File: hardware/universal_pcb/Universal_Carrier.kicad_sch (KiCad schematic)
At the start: 20 parts, among them J1 ESP32_T_LANDSCAPE, J11 PWR_ESP_5V, J12 PWR_SERVO_5V, J2 ESP32_B_LANDSCAPE, J3 SX1278_LORA_2x4, J4 BATT_APM, J5 DETECTOR_ANCORA, J6 GPS_LC29H_7PIN, SW1 UP, SW2 MODE, SW3 DOWN, SW4 BOOT

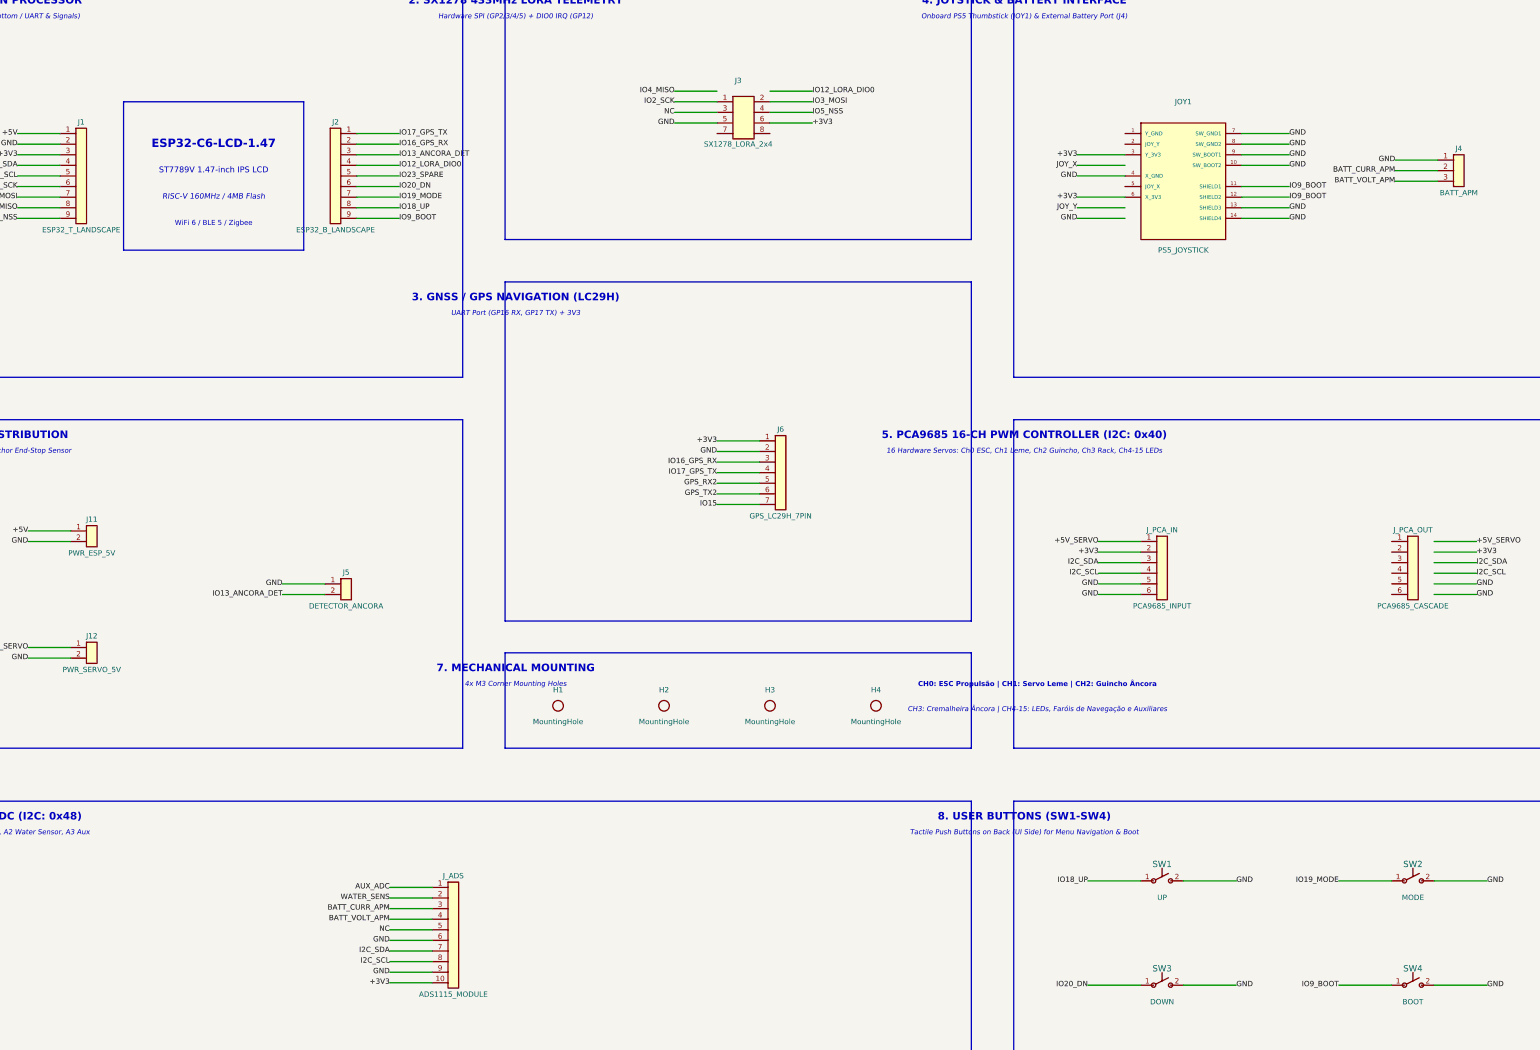
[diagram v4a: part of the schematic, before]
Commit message: feat: update Universal Carrier PCB design and gerber files with I2C cleanup
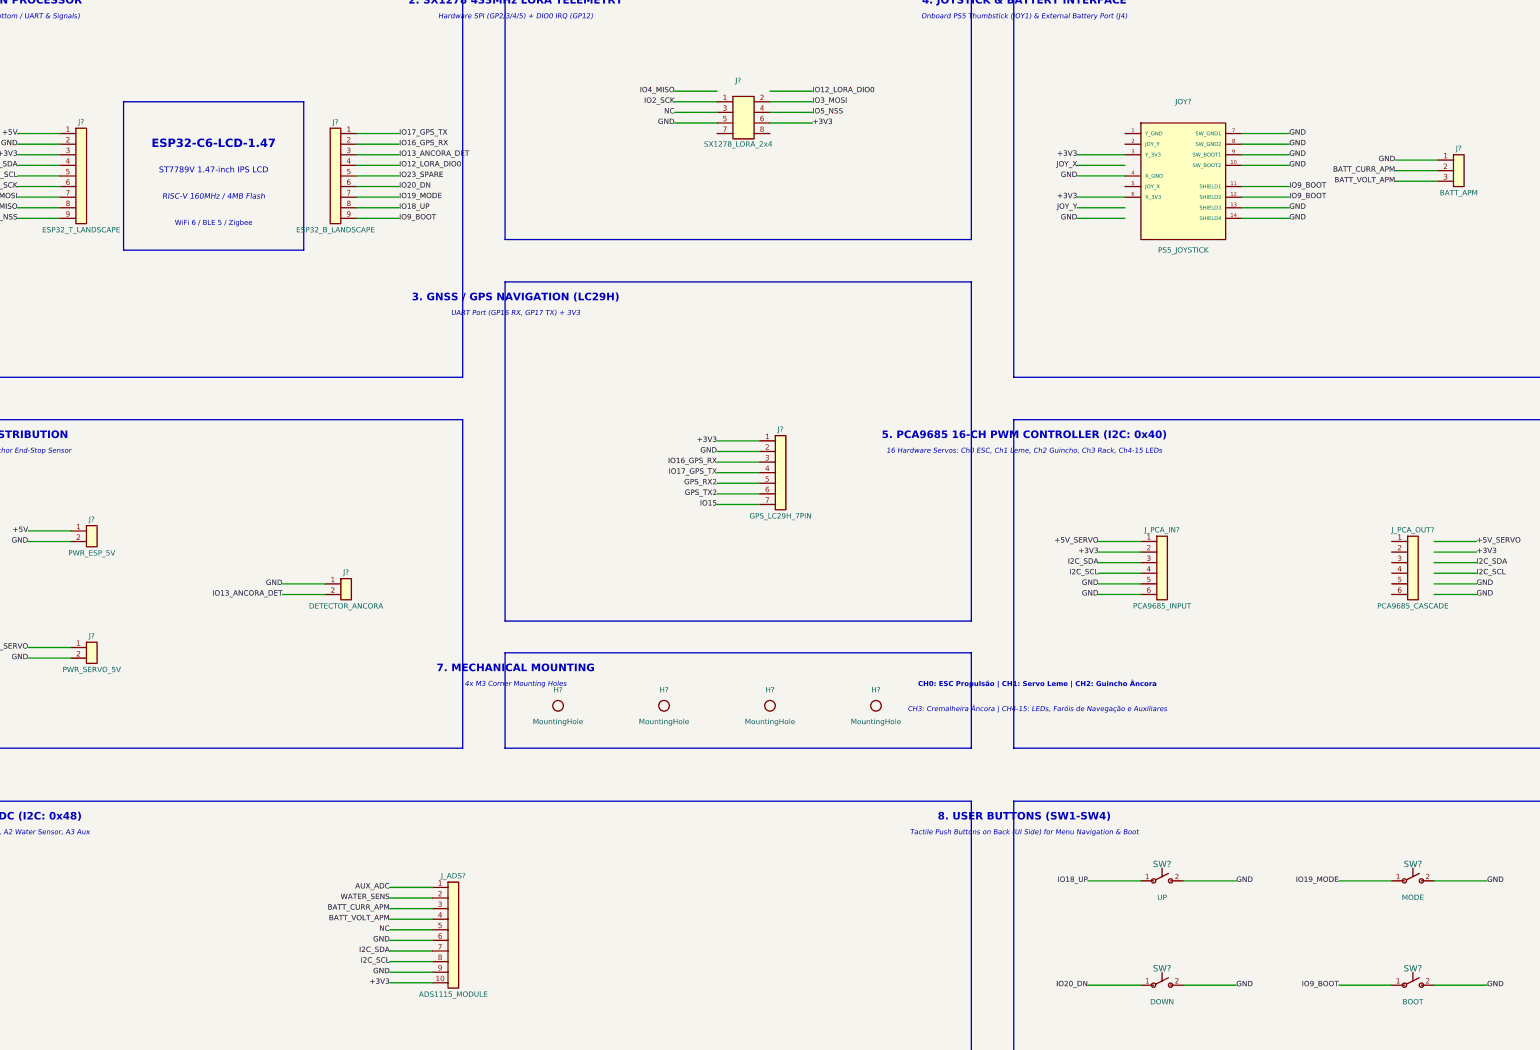
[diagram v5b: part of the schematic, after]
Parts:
- renumbered H3 to H?, H2 to H?, H4 to H?, H1 to H?, J11 to J?, J5 to J?, J6 to J?, J12 to J?, J4 to J?, J1 to J?, J2 to J?, J3 to J?, JOY1 to JOY?, J_ADS to J_ADS?, J_PCA_IN to J_PCA_IN?, J_PCA_OUT to J_PCA_OUT?, SW1 to SW?, SW2 to SW?, SW3 to SW?, SW4 to SW?
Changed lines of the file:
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@@
 		(in_pos_files yes)
 		(dnp no)
-		(property "Reference" "H3"
+		(property "Reference" "H?"
 			(at 215.9 189.23 0)
 			(show_name no)
@@
 			)
 		)
+		(instances
+			(project "Universal_Carrier"
+				(path "/c0000000-0000-0000-0000-000000000001"
+					(reference "H?")
+					(unit 1)
+				)
+			)
+		)
 	)
 	(symbol
@@
 		(in_pos_files yes)
 		(dnp no)
-		(property "Reference" "J11"
+		(property "Reference" "J?"
 			(at 53.34 148.36 0)
 			(show_name no)
@@
 		(pin "2"
 		)
+		(instances
+			(project "Universal_Carrier"
+				(path "/c0000000-0000-0000-0000-000000000001"
+					(reference "J?")
+					(unit 1)
+				)
+			)
+		)
 	)
 	(symbol
@@
 		(in_pos_files yes)
 		(dnp no)
-		(property "Reference" "H2"
+		(property "Reference" "H?"
 			(at 190.5 189.23 0)
 			(show_name no)
@@
 			)
 		)
+		(instances
+			(project "Universal_Carrier"
+				(path "/c0000000-0000-0000-0000-000000000001"
+					(reference "H?")
+					(unit 1)
+				)
+			)
+		)
 	)
 	(symbol
@@
 		(in_pos_files yes)
 		(dnp no)
-		(property "Reference" "H4"
+		(property "Reference" "H?"
 			(at 241.3 189.23 0)
 			(show_name no)
@@
 			)
 		)
+		(instances
+			(project "Universal_Carrier"
+				(path "/c0000000-0000-0000-0000-000000000001"
+					(reference "H?")
+					(unit 1)
+				)
+			)
+		)
 	)
 	(symbol
@@
 		(in_pos_files yes)
 		(dnp no)
-		(property "Reference" "SW1"
+		(property "Reference" "SW?"
 			(at 309.88 231 0)
 			(show_name no)
@@
 		(pin "2"
 		)
+		(instances
+			(project "Universal_Carrier"
+				(path "/c0000000-0000-0000-0000-000000000001"
+					(reference "SW?")
+					(unit 1)
+				)
+			)
+		)
 	)
 	(symbol
@@
 		(in_pos_files yes)
 		(dnp no)
-		(property "Reference" "J5"
+		(property "Reference" "J?"
 			(at 114.3 161.06 0)
 			(show_name no)
@@
 		(pin "2"
 		)
+		(instances
+			(project "Universal_Carrier"
+				(path "/c0000000-0000-0000-0000-000000000001"
+					(reference "J?")
+					(unit 1)
+				)
+			)
+		)
 	)
 	(symbol
@@
 		(in_pos_files yes)
 		(dnp no)
-		(property "Reference" "J6"
+		(property "Reference" "J?"
 			(at 218.44 126.77 0)
 			(show_name no)
@@
 		(pin "7"
 		)
+		(instances
+			(project "Universal_Carrier"
+				(path "/c0000000-0000-0000-0000-000000000001"
+					(reference "J?")
+					(unit 1)
+				)
+			)
+		)
 	)
 	(symbol
@@
 		(in_pos_files yes)
 		(dnp no)
-		(property "Reference" "J_ADS"
+		(property "Reference" "J_ADS?"
 			(at 140 233.8 0)
 			(show_name no)
@@
 		(pin "10"
 		)
+		(instances
+			(project "Universal_Carrier"
+				(path "/c0000000-0000-0000-0000-000000000001"
+					(reference "J_ADS?")
+					(unit 1)
+				)
+			)
+		)
 	)
 	(symbol
@@
 		(in_pos_files yes)
 		(dnp no)
-		(property "Reference" "JOY1"
+		(property "Reference" "JOY?"
 			(at 314.96 48.26 0)
 			(show_name no)
@@
 		(pin "14"
 		)
+		(instances
+			(project "Universal_Carrier"
+				(path "/c0000000-0000-0000-0000-000000000001"
+					(reference "JOY?")
+					(unit 1)
+				)
+			)
+		)
 	)
 	(symbol
@@
 		(in_pos_files yes)
 		(dnp no)
-		(property "Reference" "J_PCA_OUT"
+		(property "Reference" "J_PCA_OUT?"
 			(at 370 150.88 0)
 			(show_name no)
@@
 		(pin "6"
 		)
+		(instances
+			(project "Universal_Carrier"
+				(path "/c0000000-0000-0000-0000-000000000001"
+					(reference "J_PCA_OUT?")
+					(unit 1)
+				)
+			)
+		)
 	)
 	(symbol
@@
 		(in_pos_files yes)
 		(dnp no)
-		(property "Reference" "J12"
+		(property "Reference" "J?"
 			(at 53.34 176.3 0)
 			(show_name no)
@@
 		(pin "2"
 		)
+		(instances
+			(project "Universal_Carrier"
+				(path "/c0000000-0000-0000-0000-000000000001"
+					(reference "J?")
+					(unit 1)
+				)
+			)
+		)
 	)
 	(symbol
@@
 		(in_pos_files yes)
 		(dnp no)
-		(property "Reference" "J4"
+		(property "Reference" "J?"
 			(at 381 59.46 0)
 			(show_name no)
@@
 		(pin "3"
 		)
+		(instances
+			(project "Universal_Carrier"
+				(path "/c0000000-0000-0000-0000-000000000001"
+					(reference "J?")
+					(unit 1)
+				)
+			)
+		)
 	)
 	(symbol
@@
 		(in_pos_files yes)
 		(dnp no)
-		(property "Reference" "SW2"
+		(property "Reference" "SW?"
 			(at 370 231 0)
 			(show_name no)
@@
 		(pin "2"
 		)
+		(instances
+			(project "Universal_Carrier"
+				(path "/c0000000-0000-0000-0000-000000000001"
+					(reference "SW?")
+					(unit 1)
+				)
+			)
+		)
 	)
 	(symbol
@@
 		(in_pos_files yes)
 		(dnp no)
-		(property "Reference" "H1"
+		(property "Reference" "H?"
 			(at 165.1 189.23 0)
 			(show_name no)
@@
 			)
 		)
+		(instances
+			(project "Universal_Carrier"
+				(path "/c0000000-0000-0000-0000-000000000001"
+					(reference "H?")
+					(unit 1)
+				)
+			)
+		)
 	)
 	(symbol
@@
 		(in_pos_files yes)
 		(dnp no)
-		(property "Reference" "SW3"
+		(property "Reference" "SW?"
 			(at 309.88 256 0)
 			(show_name no)
@@
 		(pin "2"
 		)
+		(instances
+			(project "Universal_Carrier"
+				(path "/c0000000-0000-0000-0000-000000000001"
+					(reference "SW?")
+					(unit 1)
+				)
+			)
+		)
 	)
 	(symbol
@@
 		(in_pos_files yes)
 		(dnp no)
-		(property "Reference" "SW4"
+		(property "Reference" "SW?"
 			(at 370 256 0)
 			(show_name no)
@@
 		(pin "2"
 		)
+		(instances
+			(project "Universal_Carrier"
+				(path "/c0000000-0000-0000-0000-000000000001"
+					(reference "SW?")
+					(unit 1)
+				)
+			)
+		)
 	)
 	(symbol
@@
 		(in_pos_files yes)
 		(dnp no)
-		(property "Reference" "J1"
+		(property "Reference" "J?"
 			(at 50.8 53.11 0)
 			(show_name no)
@@
 		(pin "9"
 		)
+		(instances
+			(project "Universal_Carrier"
+				(path "/c0000000-0000-0000-0000-000000000001"
+					(reference "J?")
+					(unit 1)
+				)
+			)
+		)
 	)
 	(symbol
@@
 		(in_pos_files yes)
 		(dnp no)
-		(property "Reference" "J2"
+		(property "Reference" "J?"
 			(at 111.76 53.11 0)
 			(show_name no)
@@
 		(pin "9"
 		)
+		(instances
+			(project "Universal_Carrier"
+				(path "/c0000000-0000-0000-0000-000000000001"
+					(reference "J?")
+					(unit 1)
+				)
+			)
+		)
 	)
 	(symbol
@@
 		(in_pos_files yes)
 		(dnp no)
-		(property "Reference" "J3"
+		(property "Reference" "J?"
 			(at 208.28 43.18 0)
 			(show_name no)
@@
 		(pin "8"
 		)
+		(instances
+			(project "Universal_Carrier"
+				(path "/c0000000-0000-0000-0000-000000000001"
+					(reference "J?")
+					(unit 1)
+				)
+			)
+		)
 	)
 	(symbol
@@
 		(in_pos_files yes)
 		(dnp no)
-		(property "Reference" "J_PCA_IN"
+		(property "Reference" "J_PCA_IN?"
 			(at 309.88 150.88 0)
 			(show_name no)
@@
 		)
 		(pin "6"
+		)
+		(instances
+			(project "Universal_Carrier"
+				(path "/c0000000-0000-0000-0000-000000000001"
+					(reference "J_PCA_IN?")
+					(unit 1)
+				)
+			)
 		)
 	)
@@
 		)
 	)
+	(embedded_fonts no)
 )

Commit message: refactor: update base display screens and simplify navigation pages
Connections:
- net IO12_LORA_DIO0 renamed IO12_USB_DM
- net IO23_SPARE renamed IO23_LORA_DIO0
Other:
- note added: "Hardware SPI (GP2/3/4/5) + DIO0 IRQ (GP23)"
- note removed: "Hardware SPI (GP2/3/4/5) + DIO0 IRQ (GP12)"
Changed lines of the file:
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@@
 		)
 	)
-	(text "Hardware SPI (GP2/3/4/5) + DIO0 IRQ (GP12)"
+	(text "Hardware SPI (GP2/3/4/5) + DIO0 IRQ (GP23)"
 		(exclude_from_sim no)
 		(at 154.94 27.94 0)
@@
 		)
 	)
-	(label "IO12_LORA_DIO0"
+	(label "IO12_USB_DM"
 		(at 127 63.5 0)
 		(effects
@@
 		)
 	)
-	(label "IO23_SPARE"
+	(label "IO23_LORA_DIO0"
 		(at 127 66.04 0)
 		(effects
@@
 		)
 	)
-	(label "IO12_LORA_DIO0"
+	(label "IO23_LORA_DIO0"
 		(at 226.06 45.72 0)
 		(effects
